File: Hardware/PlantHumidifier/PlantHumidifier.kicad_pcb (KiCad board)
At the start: 2 copper layers, 8 parts, among them J1 110990030, J2 Conn_01x05_Female, J3 Conn_01x04_Female, J4 Conn_01x04_Female, U1 WeMos_D1_mini

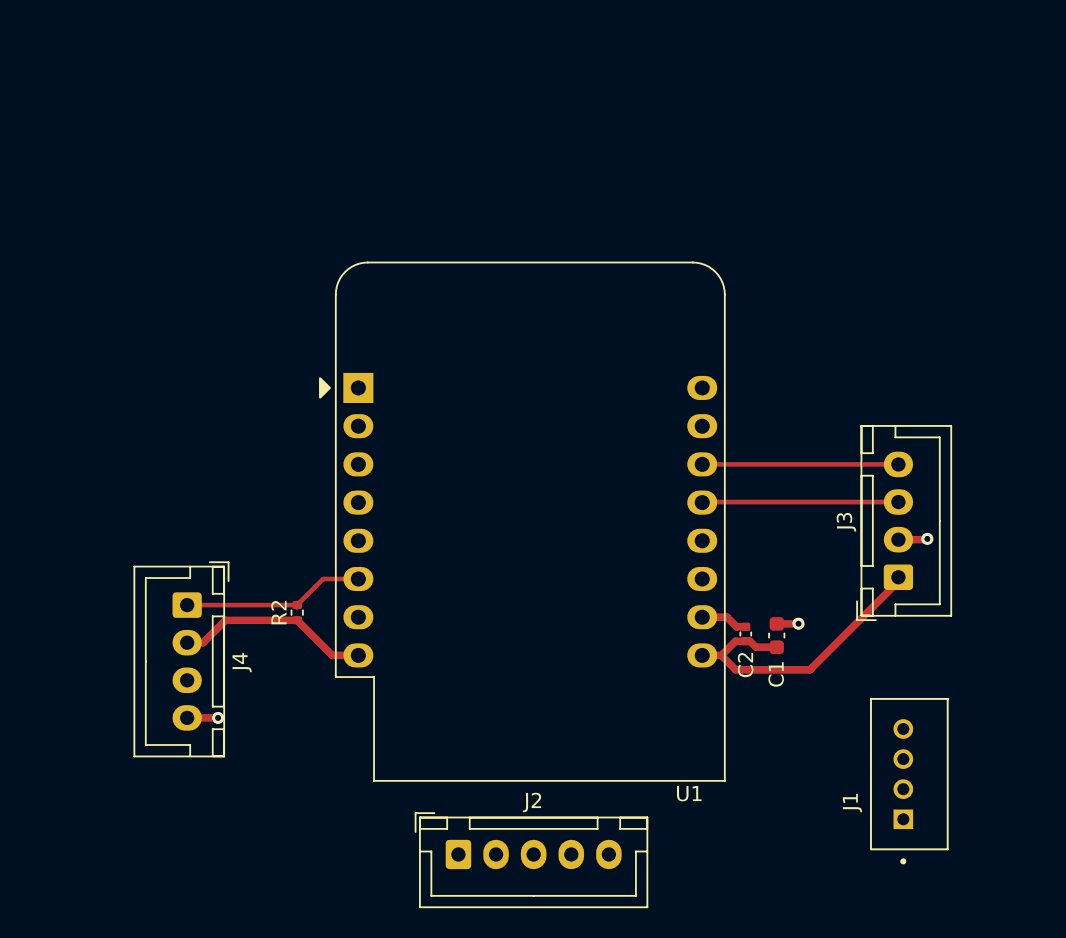
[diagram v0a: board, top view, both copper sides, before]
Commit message: Update pins again for easier routing (reflected in layout + schematic here as well)
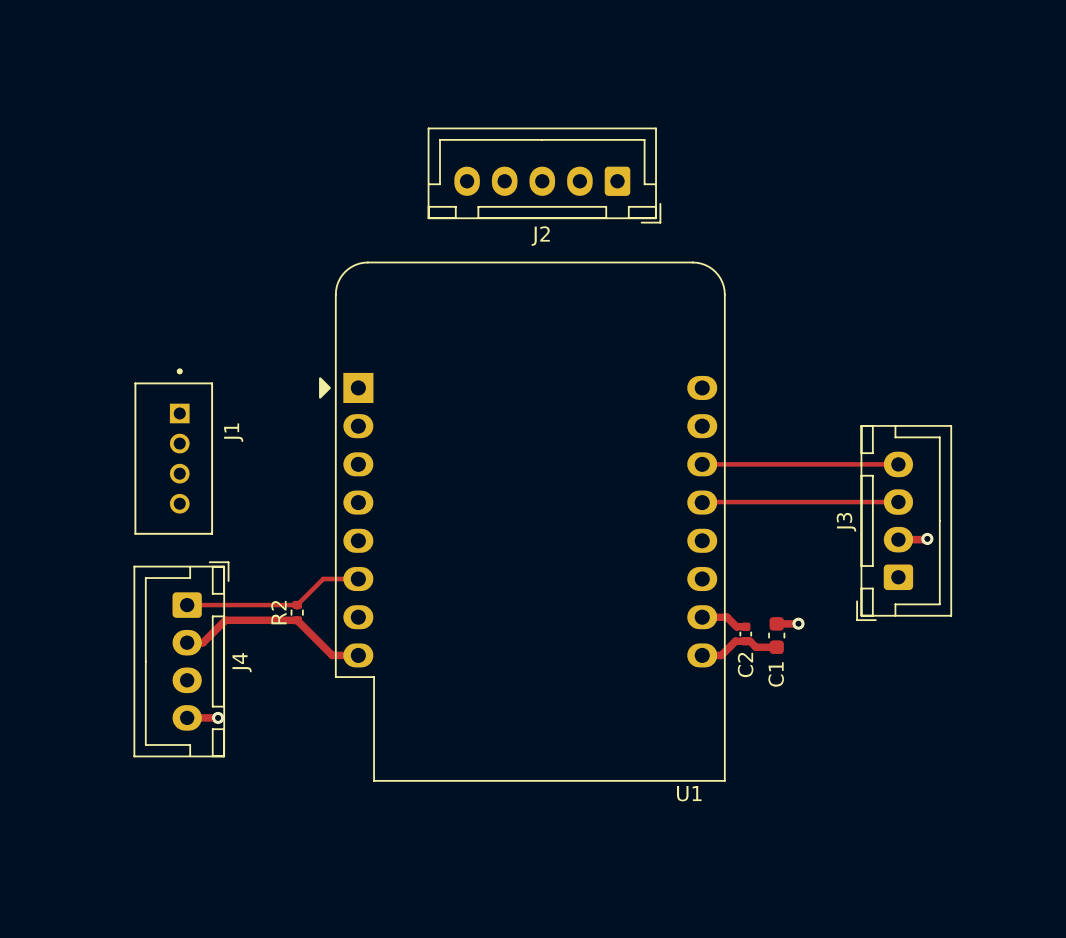
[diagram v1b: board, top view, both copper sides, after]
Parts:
- moved J1 52.5 mm to (65.7, 80.3), turned to -90 degrees
- moved J2 46.0 mm to (94.8, 61.8), turned to 180 degrees
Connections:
- J2 pad 1: /Encoder_B -> +5V
- J2 pad 2: /Encoder_A -> GND
- J2 pad 3: /Rst_n -> /Encoder_B
- J2 pad 4: +5V -> /Encoder_A
- J2 pad 5: GND -> /Rst_n
- U1 pad 3: /Atomizer -> /Encoder_A
- U1 pad 4: /Encoder_A -> /Encoder_B
- U1 pad 5: /Encoder_B -> /Atomizer
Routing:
- net +5V: track 20.4 -> 5.78 mm
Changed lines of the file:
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@@
   (net 18 "unconnected-(U1-Pad16)")
   (footprint "Connector_JST:JST_XH_B5B-XH-A_1x05_P2.50mm_Vertical" (layer "F.Cu")
-    (at 84.2264 106.5784)
+    (at 94.8 61.825 180)
     (descr "JST XH series connector, B5B-XH-A (http://www.jst-mfg.com/product/pdf/eng/eXH.pdf), generated with kicad-footprint-generator")
     (tags "connector JST XH vertical")
@@
     (fp_line (start -2.45 3.4) (end 12.45 3.4) (layer "F.Fab") (width 0.1))
     (fp_line (start -2.45 -2.35) (end -2.45 3.4) (layer "F.Fab") (width 0.1))
-    (pad "1" thru_hole roundrect (at 0 0) (size 1.7 1.95) (drill 0.95) (layers *.Cu *.Mask) (roundrect_rratio 0.147059)
-      (net 7 "/Encoder_B") (pinfunction "Pin_1") (pintype "passive"))
-    (pad "2" thru_hole oval (at 2.5 0) (size 1.7 1.95) (drill 0.95) (layers *.Cu *.Mask)
-      (net 8 "/Encoder_A") (pinfunction "Pin_2") (pintype "passive"))
-    (pad "3" thru_hole oval (at 5 0) (size 1.7 1.95) (drill 0.95) (layers *.Cu *.Mask)
-      (net 14 "/Rst_n") (pinfunction "Pin_3") (pintype "passive"))
-    (pad "4" thru_hole oval (at 7.5 0) (size 1.7 1.95) (drill 0.95) (layers *.Cu *.Mask)
-      (net 1 "+5V") (pinfunction "Pin_4") (pintype "passive"))
-    (pad "5" thru_hole oval (at 10 0) (size 1.7 1.95) (drill 0.95) (layers *.Cu *.Mask)
-      (net 2 "GND") (pinfunction "Pin_5") (pintype "passive"))
+    (pad "1" thru_hole roundrect (at 0 0 180) (size 1.7 1.95) (drill 0.95) (layers *.Cu *.Mask) (roundrect_rratio 0.147059)
+      (net 1 "+5V") (pinfunction "Pin_1") (pintype "passive"))
+    (pad "2" thru_hole oval (at 2.5 0 180) (size 1.7 1.95) (drill 0.95) (layers *.Cu *.Mask)
+      (net 2 "GND") (pinfunction "Pin_2") (pintype "passive"))
+    (pad "3" thru_hole oval (at 5 0 180) (size 1.7 1.95) (drill 0.95) (layers *.Cu *.Mask)
+      (net 7 "/Encoder_B") (pinfunction "Pin_3") (pintype "passive"))
+    (pad "4" thru_hole oval (at 7.5 0 180) (size 1.7 1.95) (drill 0.95) (layers *.Cu *.Mask)
+      (net 8 "/Encoder_A") (pinfunction "Pin_4") (pintype "passive"))
+    (pad "5" thru_hole oval (at 10 0 180) (size 1.7 1.95) (drill 0.95) (layers *.Cu *.Mask)
+      (net 14 "/Rst_n") (pinfunction "Pin_5") (pintype "passive"))
     (model "${KICAD6_3DMODEL_DIR}/Connector_JST.3dshapes/JST_XH_B5B-XH-A_1x05_P2.50mm_Vertical.wrl"
       (offset (xyz 0 0 0))
@@
       (net 15 "unconnected-(U1-Pad2)") (pinfunction "A0") (pintype "input+no_connect"))
     (pad "3" thru_hole oval (at 0 5.08) (size 2 1.6) (drill 1) (layers *.Cu *.Mask)
-      (net 3 "/Atomizer") (pinfunction "D0") (pintype "bidirectional"))
+      (net 8 "/Encoder_A") (pinfunction "D0") (pintype "bidirectional"))
     (pad "4" thru_hole oval (at 0 7.62) (size 2 1.6) (drill 1) (layers *.Cu *.Mask)
-      (net 8 "/Encoder_A") (pinfunction "SCK/D5") (pintype "bidirectional"))
+      (net 7 "/Encoder_B") (pinfunction "SCK/D5") (pintype "bidirectional"))
     (pad "5" thru_hole oval (at 0 10.16) (size 2 1.6) (drill 1) (layers *.Cu *.Mask)
-      (net 7 "/Encoder_B") (pinfunction "MISO/D6") (pintype "bidirectional"))
+      (net 3 "/Atomizer") (pinfunction "MISO/D6") (pintype "bidirectional"))
     (pad "6" thru_hole oval (at 0 12.7) (size 2 1.6) (drill 1) (layers *.Cu *.Mask)
       (net 11 "/DHT22_Sense") (pinfunction "MOSI/D7") (pintype "bidirectional"))
@@
   )
   (footprint "Seeed_Connectors:SEEED_110990030" (layer "F.Cu")
-    (at 113.8 101.2375 90)
+    (at 65.7 80.2625 -90)
     (property "MANUFACTURER" "Seeed Technology")
     (property "MAXIMUM_PACKAGE_HEIGHT" "8.1mm")
@@
     (fp_line (start -5 2.95) (end -5 -2.15) (layer "F.Fab") (width 0.127))
     (fp_circle (center -5.8 0) (end -5.7 0) (layer "F.Fab") (width 0.2) (fill none))
-    (pad "1" thru_hole rect locked (at -3 0 90) (size 1.308 1.308) (drill 0.8) (layers *.Cu *.Mask)
+    (pad "1" thru_hole rect locked (at -3 0 270) (size 1.308 1.308) (drill 0.8) (layers *.Cu *.Mask)
       (net 3 "/Atomizer") (pinfunction "1") (pintype "passive"))
-    (pad "2" thru_hole circle locked (at -1 0 90) (size 1.308 1.308) (drill 0.8) (layers *.Cu *.Mask)
+    (pad "2" thru_hole circle locked (at -1 0 270) (size 1.308 1.308) (drill 0.8) (layers *.Cu *.Mask)
       (net 4 "unconnected-(J1-Pad2)") (pinfunction "2") (pintype "passive+no_connect"))
-    (pad "3" thru_hole circle locked (at 1 0 90) (size 1.308 1.308) (drill 0.8) (layers *.Cu *.Mask)
+    (pad "3" thru_hole circle locked (at 1 0 270) (size 1.308 1.308) (drill 0.8) (layers *.Cu *.Mask)
       (net 1 "+5V") (pinfunction "3") (pintype "passive"))
-    (pad "4" thru_hole circle locked (at 3 0 90) (size 1.308 1.308) (drill 0.8) (layers *.Cu *.Mask)
+    (pad "4" thru_hole circle locked (at 3 0 270) (size 1.308 1.308) (drill 0.8) (layers *.Cu *.Mask)
       (net 2 "GND") (pinfunction "4") (pintype "passive"))
   )
   (segment (start 103.3272 92.4026) (end 103.604 92.4026) (width 0.5) (layer "F.Cu") (net 1))
-  (segment (start 113.475 88.425) (end 107.6 94.3) (width 0.5) (layer "F.Cu") (net 1))
-  (segment (start 102.6566 94.3) (end 101.7016 93.345) (width 0.5) (layer "F.Cu") (net 1))
-  (segment (start 107.6 94.3) (end 102.6566 94.3) (width 0.5) (layer "F.Cu") (net 1))
   (segment (start 104.0006 92.7992) (end 105.3846 92.7992) (width 0.5) (layer "F.Cu") (net 1))
   (segment (start 103.604 92.4026) (end 104.0006 92.7992) (width 0.5) (layer "F.Cu") (net 1))

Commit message: Layout: Route encoder and atomizer
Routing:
- net /Encoder_B: track 0.00 -> 40.8 mm
- net /Encoder_A: track 0.00 -> 33.0 mm
- net /Rst_n: track 0.00 -> 21.5 mm
- net /Atomizer: track 0.00 -> 15.4 mm
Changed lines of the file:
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@@
   (via (at 106.8324 91.2368) (size 0.8) (drill 0.4) (layers "F.Cu" "B.Cu") (net 2))
   (via (at 115.4 85.6) (size 0.8) (drill 0.4) (layers "F.Cu" "B.Cu") (net 2))
+  (segment (start 65.7 77.2625) (end 66.4625 77.2625) (width 0.3) (layer "F.Cu") (net 3))
+  (segment (start 66.4625 77.2625) (end 74.925 85.725) (width 0.3) (layer "F.Cu") (net 3))
+  (segment (start 74.925 85.725) (end 77.574 85.725) (width 0.3) (layer "F.Cu") (net 3))
   (segment (start 100.469 83.15) (end 100.434 83.185) (width 0.3) (layer "F.Cu") (net 5))
   (segment (start 113.475 83.15) (end 100.469 83.15) (width 0.3) (layer "F.Cu") (net 5))
   (segment (start 113.47 80.645) (end 113.475 80.65) (width 0.3) (layer "F.Cu") (net 6))
   (segment (start 100.434 80.645) (end 113.47 80.645) (width 0.3) (layer "F.Cu") (net 6))
+  (segment (start 72.3 77.911) (end 77.574 83.185) (width 0.3) (layer "F.Cu") (net 7))
+  (segment (start 80.5 59) (end 72.3 67.2) (width 0.3) (layer "F.Cu") (net 7))
+  (segment (start 88 59) (end 80.5 59) (width 0.3) (layer "F.Cu") (net 7))
+  (segment (start 72.3 67.2) (end 72.3 77.911) (width 0.3) (layer "F.Cu") (net 7))
+  (segment (start 89.8 60.8) (end 88 59) (width 0.3) (layer "F.Cu") (net 7))
+  (segment (start 89.8 61.825) (end 89.8 60.8) (width 0.3) (layer "F.Cu") (net 7))
+  (segment (start 73.6 67.2) (end 73.6 76.671) (width 0.3) (layer "F.Cu") (net 8))
+  (segment (start 87.3 60.8) (end 86.6 60.1) (width 0.3) (layer "F.Cu") (net 8))
+  (segment (start 87.3 61.825) (end 87.3 60.8) (width 0.3) (layer "F.Cu") (net 8))
+  (segment (start 73.6 76.671) (end 77.574 80.645) (width 0.3) (layer "F.Cu") (net 8))
+  (segment (start 80.7 60.1) (end 73.6 67.2) (width 0.3) (layer "F.Cu") (net 8))
+  (segment (start 86.6 60.1) (end 80.7 60.1) (width 0.3) (layer "F.Cu") (net 8))
   (segment (start 68.74 91.01) (end 73.5076 91.01) (width 0.5) (layer "F.Cu") (net 10))
   (segment (start 73.5076 91.01) (end 75.8426 93.345) (width 0.5) (layer "F.Cu") (net 10))
@@
   (segment (start 66.1924 90) (end 73.4976 90) (width 0.3) (layer "F.Cu") (net 11))
   (segment (start 73.3396 90) (end 73.5076 90.168) (width 0.3) (layer "F.Cu") (net 11))
+  (segment (start 76.965 75.565) (end 77.574 75.565) (width 0.3) (layer "F.Cu") (net 14))
+  (segment (start 75.2 73.8) (end 76.965 75.565) (width 0.3) (layer "F.Cu") (net 14))
+  (segment (start 75.2 67.3) (end 75.2 73.8) (width 0.3) (layer "F.Cu") (net 14))
+  (segment (start 80.675 61.825) (end 75.2 67.3) (width 0.3) (layer "F.Cu") (net 14))
+  (segment (start 84.8 61.825) (end 80.675 61.825) (width 0.3) (layer "F.Cu") (net 14))
 )
